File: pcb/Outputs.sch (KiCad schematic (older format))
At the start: 18 parts, among them Q10 VNN7NV0413TR, Q11 VNN7NV0413TR, Q9 VNN7NV0413TR

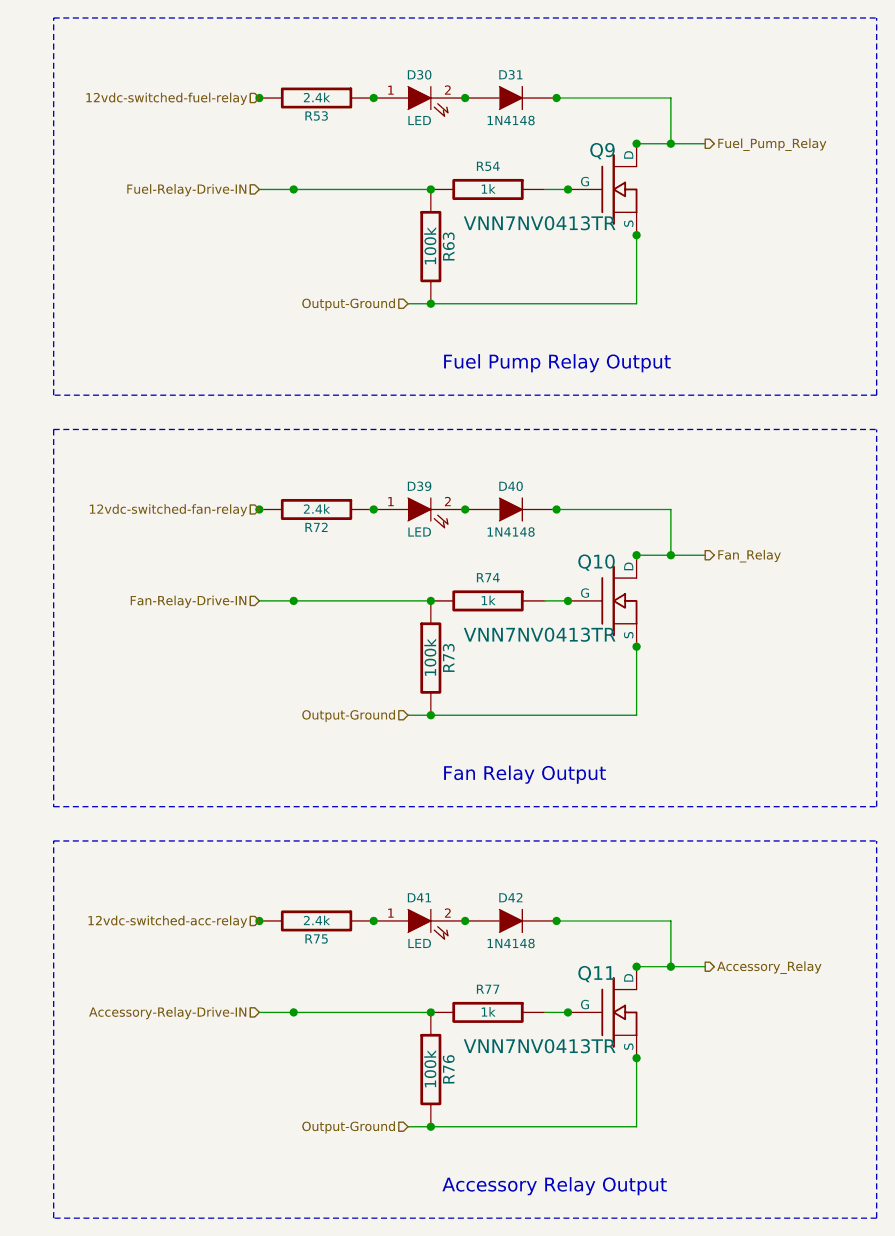
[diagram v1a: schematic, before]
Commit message: Updated schematics, PDFs and PNGs with lumpensack2003 suggestions
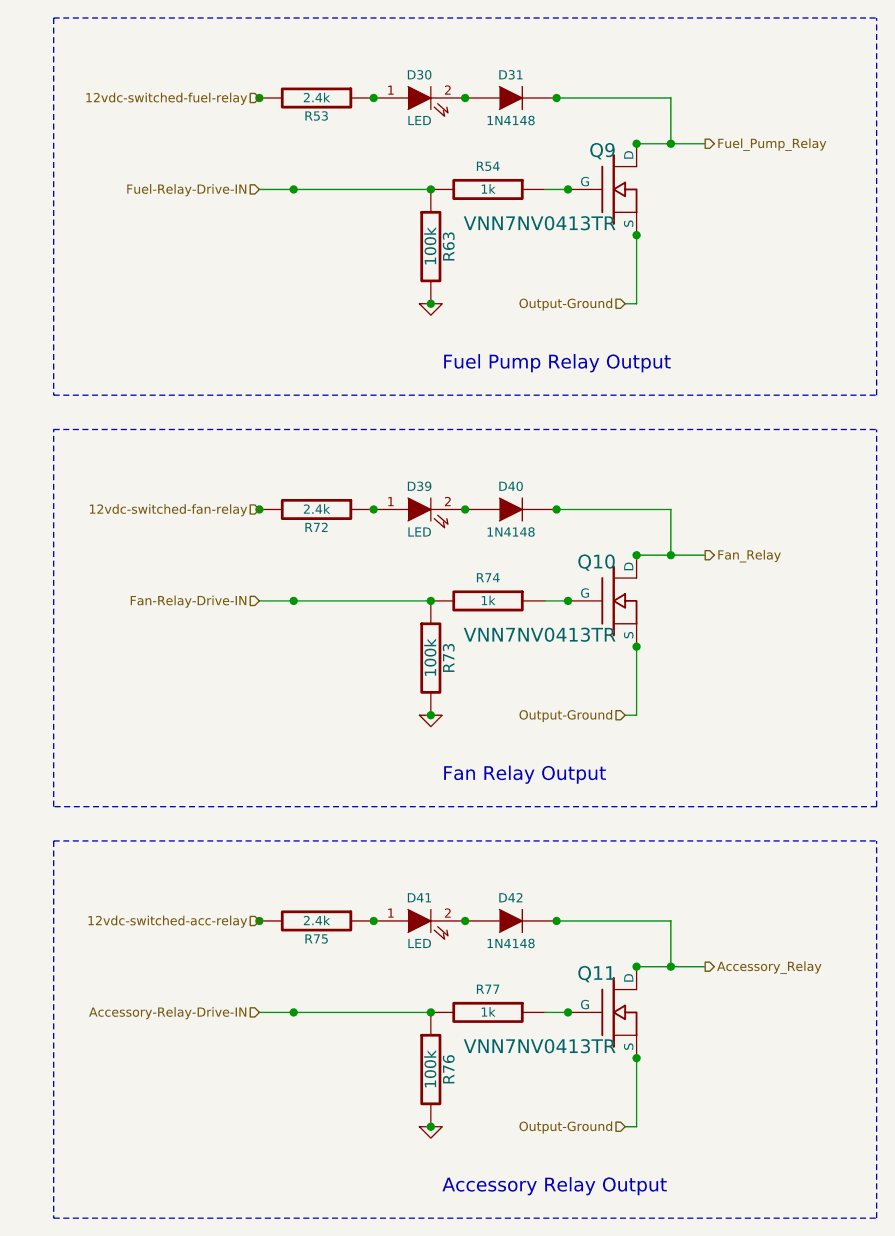
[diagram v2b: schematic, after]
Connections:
- net Output-Ground: no longer R63.2, R73.2, R76.2
- new net GND: R63.2, R73.2, R76.2
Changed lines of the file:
@@
-EESchema Schematic File Version 2  date Sun 05 Feb 2012 11:20:52 AM EST
+EESchema Schematic File Version 2  date Sun 05 Feb 2012 10:59:48 PM EST
+LIBS:opto
+LIBS:Jaguar
 LIBS:power
-LIBS:device
-LIBS:transistors
-LIBS:conn
-LIBS:linear
-LIBS:regul
-LIBS:74xx
-LIBS:analog_switches
-LIBS:interface
-LIBS:opto
-LIBS:contrib
-LIBS:Jaguar
 LIBS:Jaguar-cache
 EELAYER 24  0
@@
 Sheet 5 7
 Title "Jaguar PCB for FreeEMS"
-Date "5 feb 2012"
+Date "6 feb 2012"
 Rev "A.2"
 Comp "diyefi.org"
@@
 Comment4 ""
 $EndDescr
-Text HLabel 5350 5650 0    40   Input ~ 0
+$Comp
+L GND #PWR060
+U 1 1 4F2F3E3F
+P 5450 5650
+F 0 "#PWR060" H 5450 5650 30  0001 C CNN
+F 1 "GND" H 5450 5580 30  0001 C CNN
+	1    5450 5650
+	1    0    0    -1
+$EndComp
+Wire Wire Line
+	6300 5650 6350 5650
+Wire Wire Line
+	5450 1550 4700 1550
+Wire Notes Line
+	3800 800  7400 800
+Wire Notes Line
+	3800 800  3800 2450
+Wire Notes Line
+	3800 2450 7400 2450
+Wire Notes Line
+	7400 2450 7400 800
+Wire Wire Line
+	6500 1350 6500 1150
+Wire Wire Line
+	6350 1350 6650 1350
+Connection ~ 6500 1350
+Connection ~ 6350 1350
+Connection ~ 6350 1750
+Connection ~ 6050 1550
+Connection ~ 5200 1150
+Connection ~ 4700 1150
+Connection ~ 5600 1150
+Connection ~ 6000 1150
+Wire Wire Line
+	6500 1150 6000 1150
+Wire Wire Line
+	6350 1750 6350 2050
+Connection ~ 5450 2050
+Connection ~ 5450 1550
+Wire Wire Line
+	5950 1550 6050 1550
+Connection ~ 4850 1550
+Connection ~ 4850 3350
+Wire Wire Line
+	5950 3350 6050 3350
+Connection ~ 5450 3350
+Connection ~ 5450 3850
+Wire Wire Line
+	6350 3550 6350 3850
+Wire Wire Line
+	6000 2950 6500 2950
+Connection ~ 6000 2950
+Connection ~ 5600 2950
+Connection ~ 4700 2950
+Connection ~ 5200 2950
+Connection ~ 6050 3350
+Connection ~ 6350 3550
+Connection ~ 6350 3150
+Connection ~ 6500 3150
+Wire Wire Line
+	6350 3150 6650 3150
+Wire Wire Line
+	6500 2950 6500 3150
+Wire Notes Line
+	7400 4250 7400 2600
+Wire Notes Line
+	7400 4250 3800 4250
+Wire Notes Line
+	3800 4250 3800 2600
+Wire Notes Line
+	3800 2600 7400 2600
+Wire Wire Line
+	5450 3350 4700 3350
+Wire Wire Line
+	5450 5150 4700 5150
+Wire Notes Line
+	3800 4400 7400 4400
+Wire Notes Line
+	3800 4400 3800 6050
+Wire Notes Line
+	3800 6050 7400 6050
+Wire Notes Line
+	7400 6050 7400 4400
+Wire Wire Line
+	6500 4950 6500 4750
+Wire Wire Line
+	6350 4950 6650 4950
+Connection ~ 6500 4950
+Connection ~ 6350 4950
+Connection ~ 6350 5350
+Connection ~ 6050 5150
+Connection ~ 5200 4750
+Connection ~ 4700 4750
+Connection ~ 5600 4750
+Connection ~ 6000 4750
+Wire Wire Line
+	6500 4750 6000 4750
+Wire Wire Line
+	6350 5650 6350 5350
+Connection ~ 5450 5650
+Connection ~ 5450 5150
+Wire Wire Line
+	5950 5150 6050 5150
+Connection ~ 4850 5150
+Wire Wire Line
+	6350 2050 6300 2050
+Wire Wire Line
+	6350 3850 6300 3850
+$Comp
+L GND #PWR061
+U 1 1 4F2F3E2D
+P 5450 3850
+F 0 "#PWR061" H 5450 3850 30  0001 C CNN
+F 1 "GND" H 5450 3780 30  0001 C CNN
+	1    5450 3850
+	1    0    0    -1
+$EndComp
+$Comp
+L GND #PWR062
+U 1 1 4F2F3E0C
+P 5450 2050
+F 0 "#PWR062" H 5450 2050 30  0001 C CNN
+F 1 "GND" H 5450 1980 30  0001 C CNN
+	1    5450 2050
+	1    0    0    -1
+$EndComp
+Text HLabel 6300 5650 0    40   Input ~ 0
 Output-Ground
 $Comp
@@
 	0    1    1    0
 $EndComp
-Connection ~ 4850 5150
-Wire Wire Line
-	5950 5150 6050 5150
-Wire Wire Line
-	5350 5650 6350 5650
-Connection ~ 5450 5150
-Connection ~ 5450 5650
-Wire Wire Line
-	6350 5650 6350 5350
-Wire Wire Line
-	6000 4750 6500 4750
-Connection ~ 6000 4750
-Connection ~ 5600 4750
-Connection ~ 4700 4750
-Connection ~ 5200 4750
-Connection ~ 6050 5150
-Connection ~ 6350 5350
-Connection ~ 6350 4950
-Connection ~ 6500 4950
-Wire Wire Line
-	6350 4950 6650 4950
-Wire Wire Line
-	6500 4750 6500 4950
-Wire Notes Line
-	7400 6050 7400 4400
-Wire Notes Line
-	7400 6050 3800 6050
-Wire Notes Line
-	3800 6050 3800 4400
-Wire Notes Line
-	3800 4400 7400 4400
-Wire Wire Line
-	5450 5150 4700 5150
-Wire Wire Line
-	5450 3350 4700 3350
-Wire Notes Line
-	3800 2600 7400 2600
-Wire Notes Line
-	3800 2600 3800 4250
-Wire Notes Line
-	3800 4250 7400 4250
-Wire Notes Line
-	7400 4250 7400 2600
-Wire Wire Line
-	6500 3150 6500 2950
-Wire Wire Line
-	6350 3150 6650 3150
-Connection ~ 6500 3150
-Connection ~ 6350 3150
-Connection ~ 6350 3550
-Connection ~ 6050 3350
-Connection ~ 5200 2950
-Connection ~ 4700 2950
-Connection ~ 5600 2950
-Connection ~ 6000 2950
-Wire Wire Line
-	6500 2950 6000 2950
-Wire Wire Line
-	6350 3550 6350 3850
-Connection ~ 5450 3850
-Connection ~ 5450 3350
-Wire Wire Line
-	6350 3850 5350 3850
-Wire Wire Line
-	5950 3350 6050 3350
-Connection ~ 4850 3350
-Connection ~ 4850 1550
-Wire Wire Line
-	5950 1550 6050 1550
-Wire Wire Line
-	5350 2050 6350 2050
-Connection ~ 5450 1550
-Connection ~ 5450 2050
-Wire Wire Line
-	6350 2050 6350 1750
-Wire Wire Line
-	6000 1150 6500 1150
-Connection ~ 6000 1150
-Connection ~ 5600 1150
-Connection ~ 4700 1150
-Connection ~ 5200 1150
-Connection ~ 6050 1550
-Connection ~ 6350 1750
-Connection ~ 6350 1350
-Connection ~ 6500 1350
-Wire Wire Line
-	6350 1350 6650 1350
-Wire Wire Line
-	6500 1150 6500 1350
-Wire Notes Line
-	7400 2450 7400 800
-Wire Notes Line
-	7400 2450 3800 2450
-Wire Notes Line
-	3800 2450 3800 800
-Wire Notes Line
-	3800 800  7400 800
-Wire Wire Line
-	5450 1550 4700 1550
 $Comp
 L R R74
@@
 	1    0    0    -1
 $EndComp
-Text HLabel 5350 3850 0    40   Input ~ 0
+Text HLabel 6300 3850 0    40   Input ~ 0
 Output-Ground
-Text HLabel 5350 2050 0    40   Input ~ 0
+Text HLabel 6300 2050 0    40   Input ~ 0
 Output-Ground
 $Comp
